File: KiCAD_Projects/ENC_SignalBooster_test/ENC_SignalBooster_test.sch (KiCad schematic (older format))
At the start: 12 parts, among them P1 CONN_01X04, P2 CONN_01X04, U1 74HC04

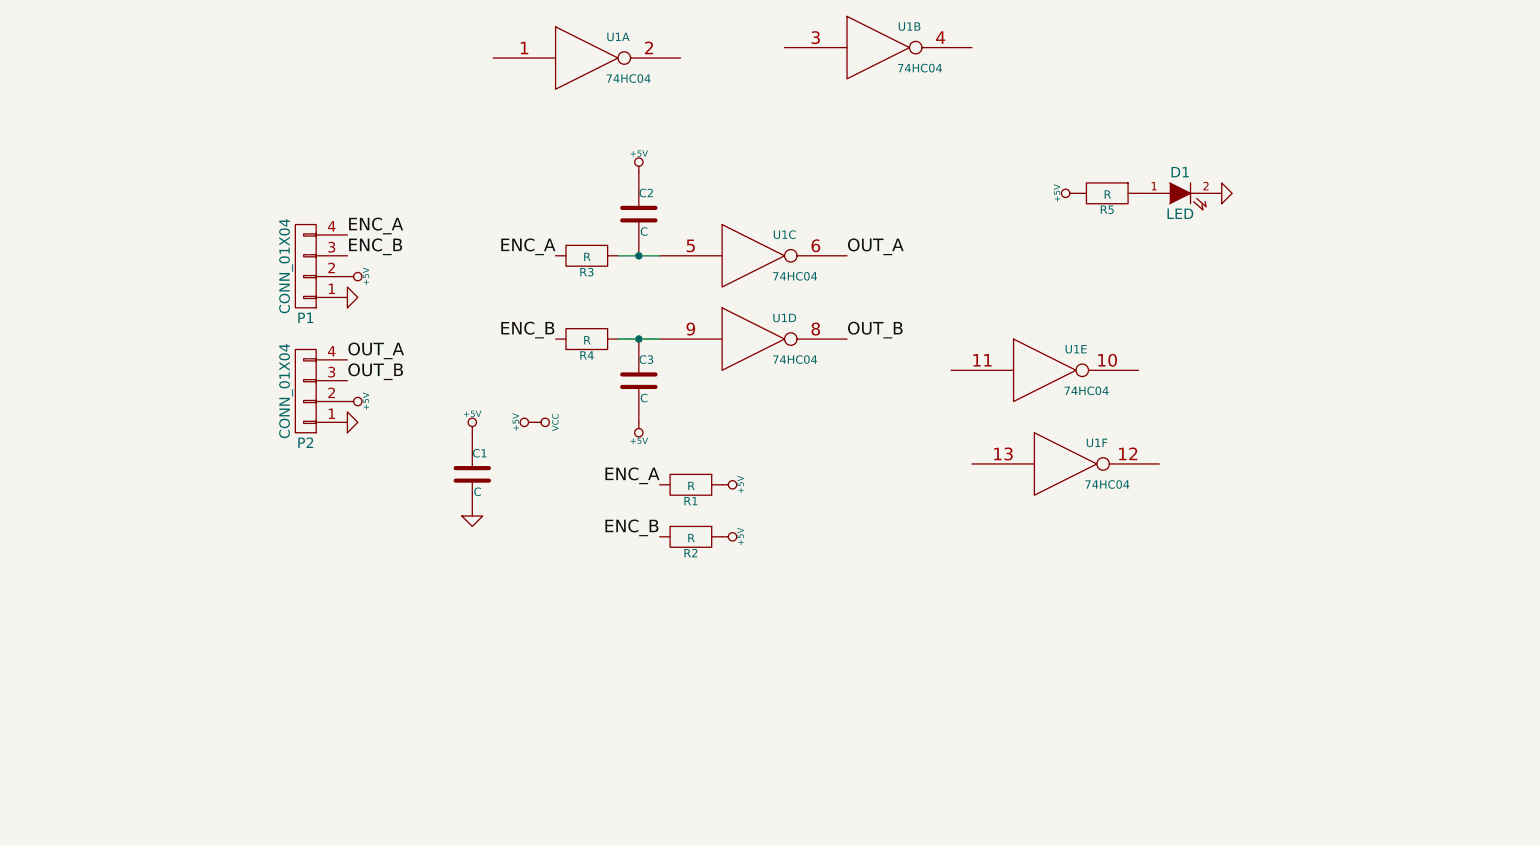
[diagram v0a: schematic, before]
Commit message: 明日の加工用データの出力､Cancer用電源基板の再設計
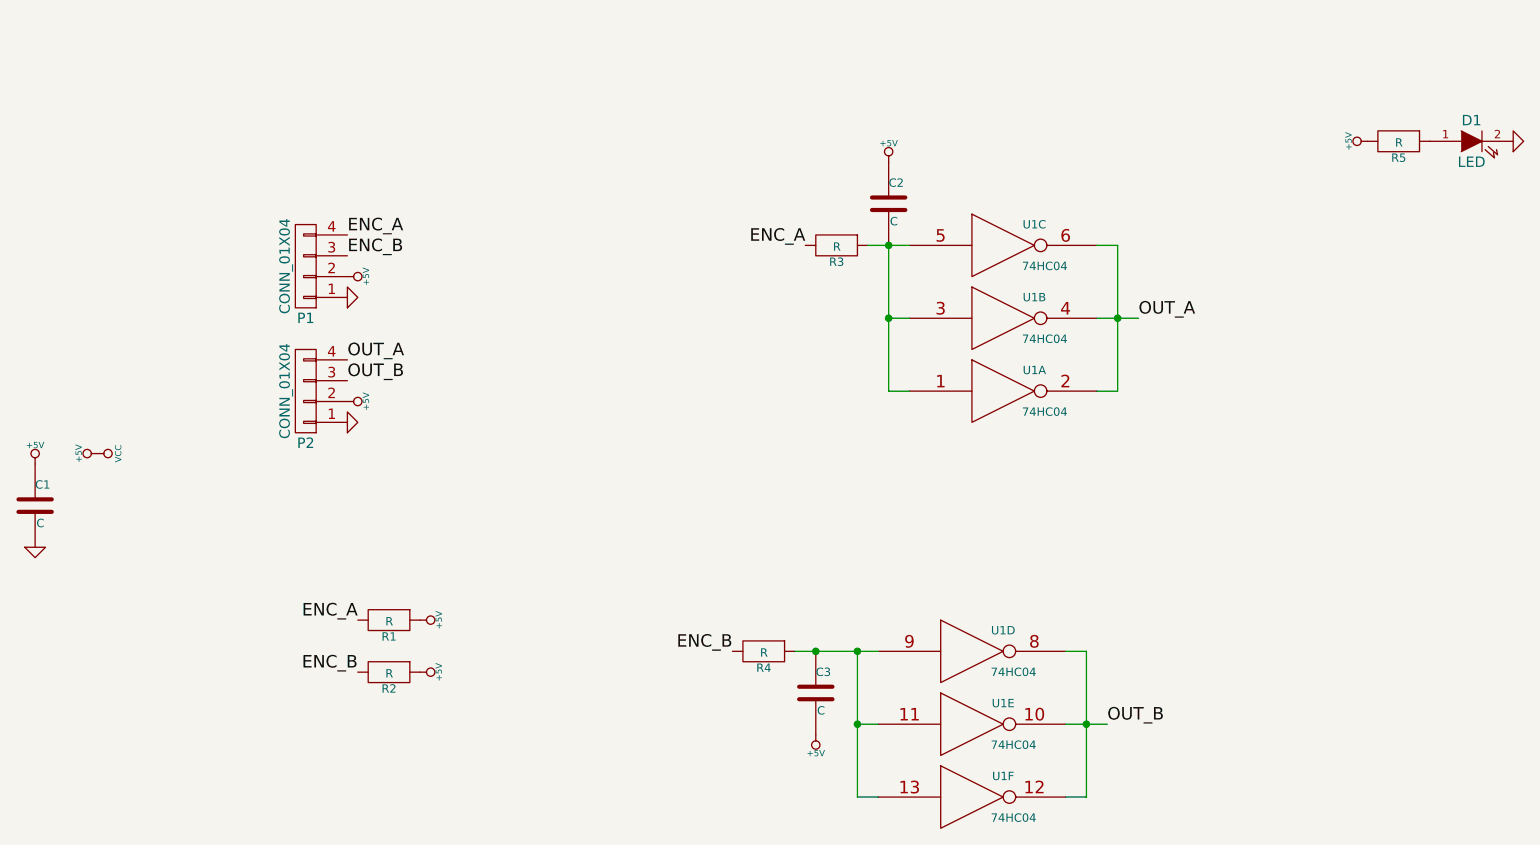
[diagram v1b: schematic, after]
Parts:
- C1, C3, D1, R1, R2, R3, R4, R5: footprint RP_KiCAD_Libs:C1608_WP -> RP_KiCAD_Libs:C1608_NP
- C2: footprint RP_KiCAD_Libs:C1608 -> RP_KiCAD_Libs:C1608_NP
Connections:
- net OUT_A: now also U1.2, U1.4
- net OUT_B: now also U1.10, U1.12
- net at U1.3: now also C2.2, R3.1, U1.1, U1.5
- net at C3.1, R4.1, U1.9: now also U1.11, U1.13
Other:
- moved on the sheet: C1, C2, C3, D1, R1, R2, R3, R4, R5, U1A, U1B, U1C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
